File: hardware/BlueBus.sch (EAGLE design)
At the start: 76 parts

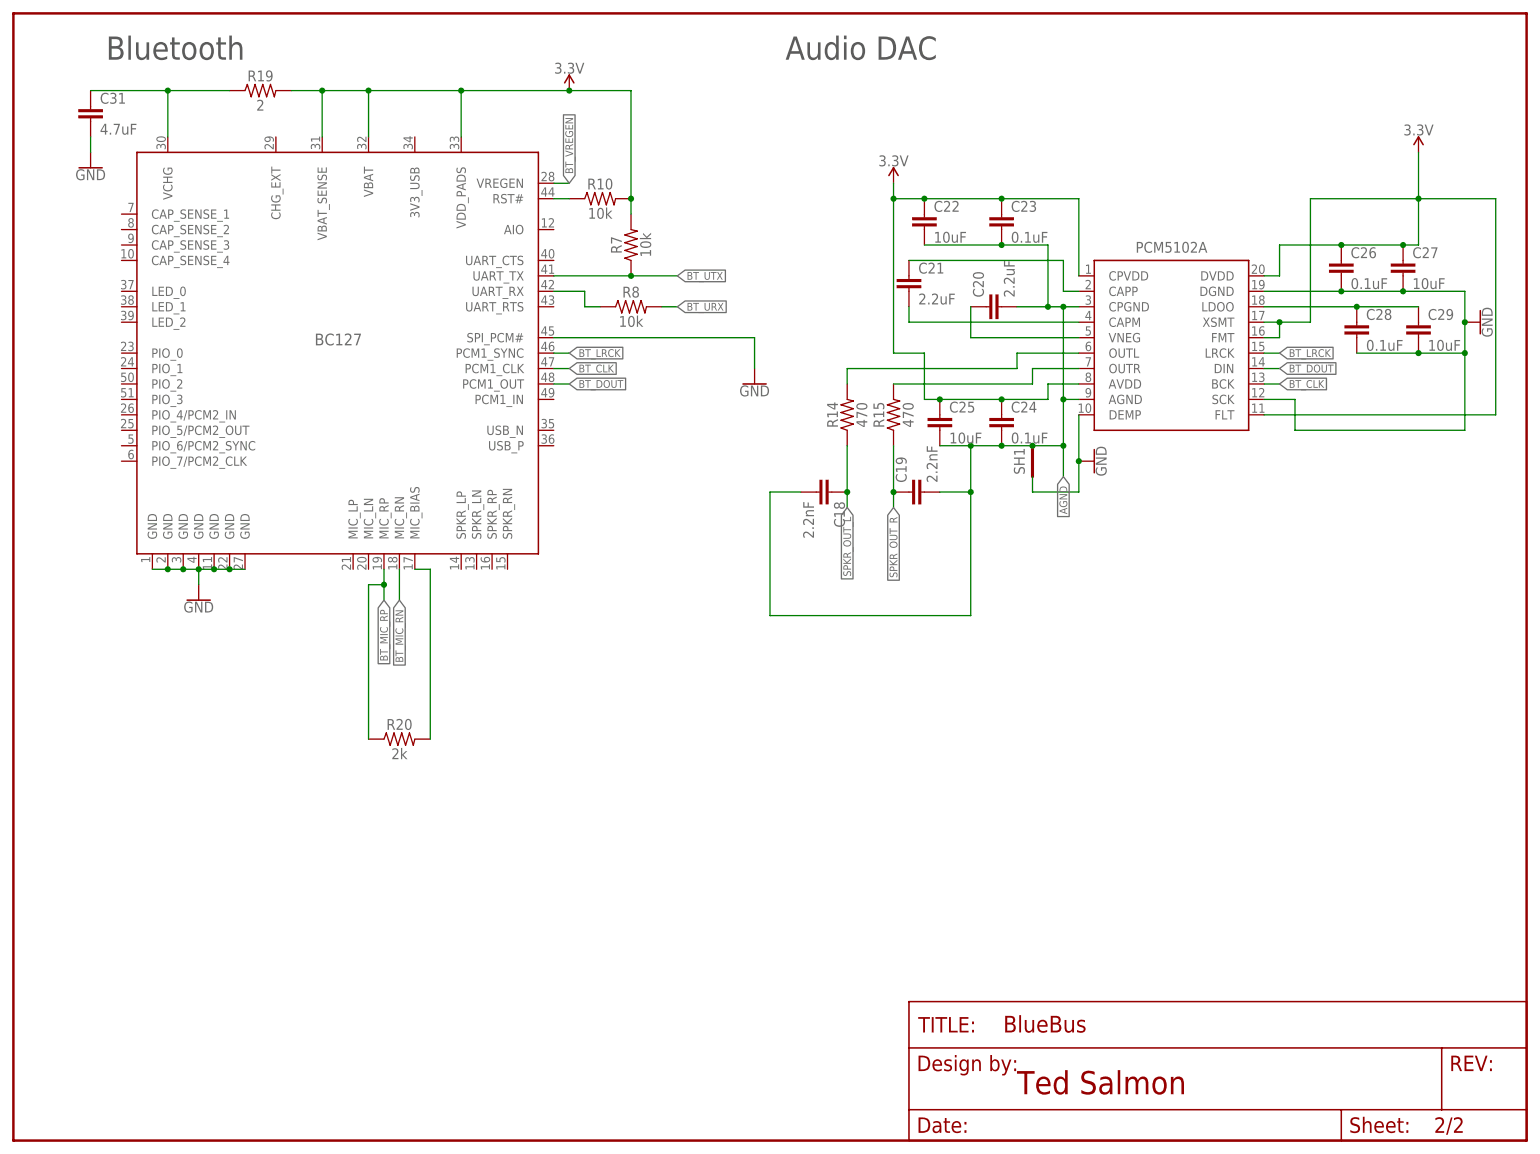
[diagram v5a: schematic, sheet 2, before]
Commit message: [IMP] hardware: MIC IN Fixes
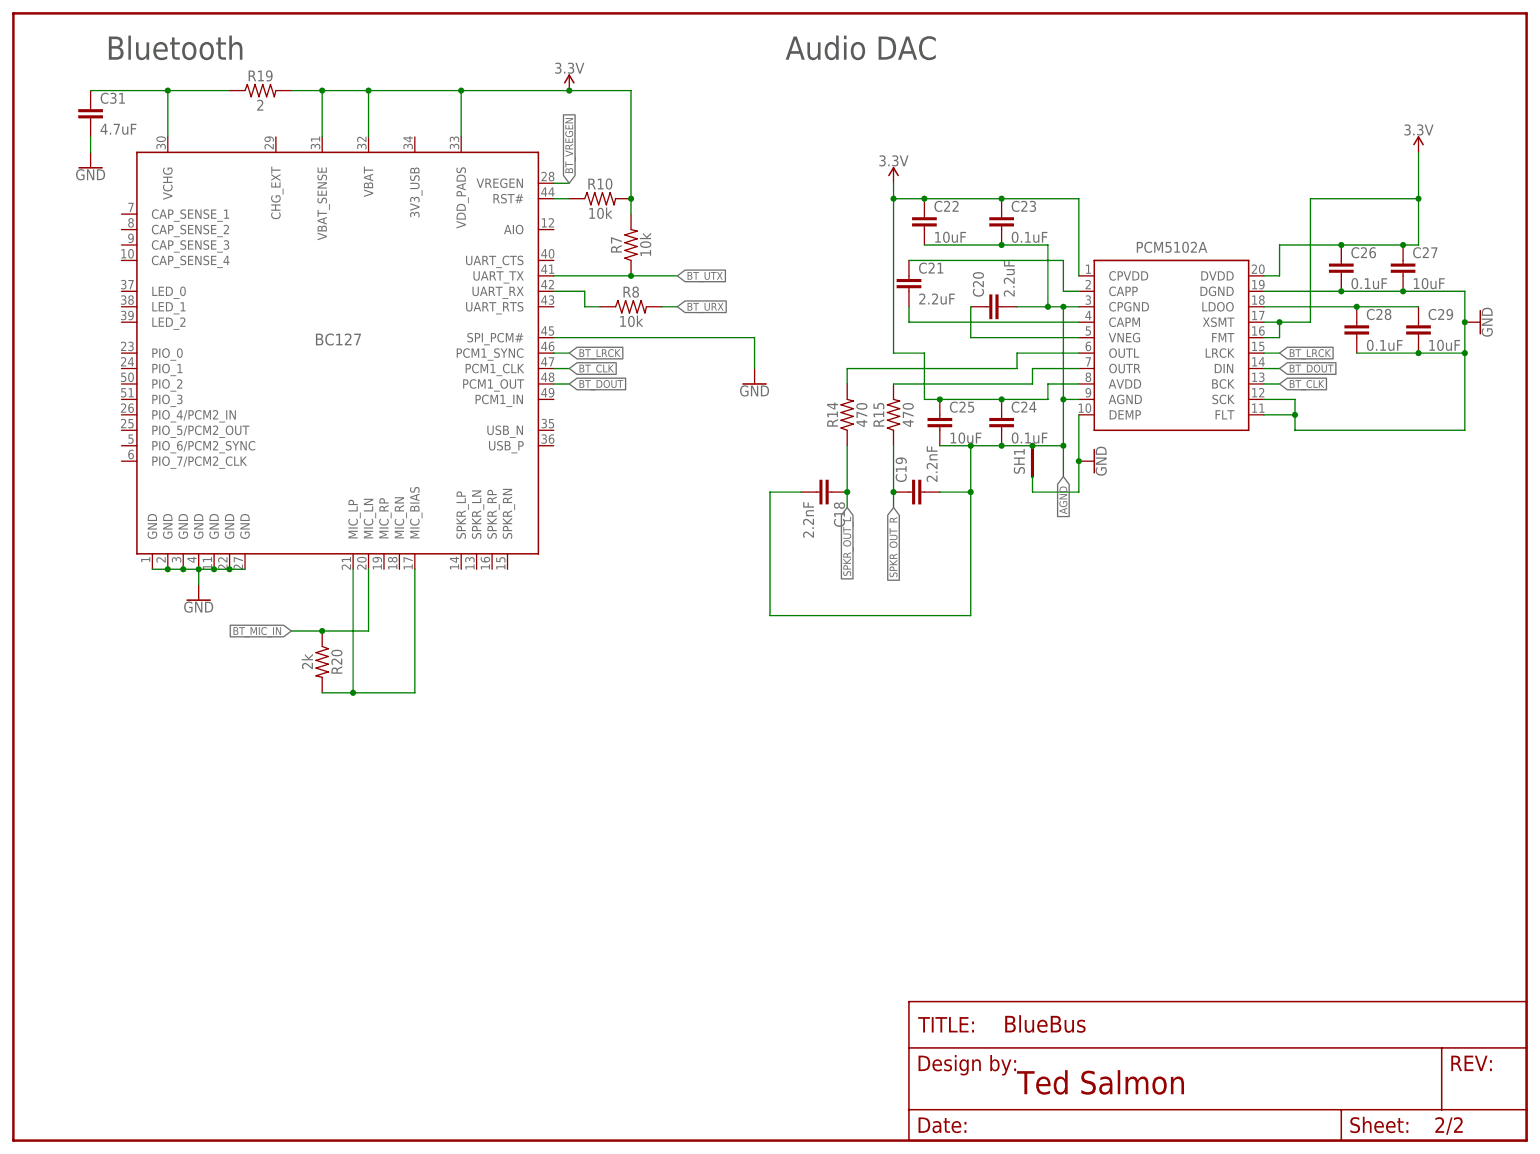
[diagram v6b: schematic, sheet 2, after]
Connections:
- removed net BT_MIC_BIAS: BC127.MIC_BIAS, R20.2
- removed net BT_MIC_RN: BC127.MIC_RN, MIC_IN.2
- removed net BT_MIC_RP: BC127.MIC_RP, MIC_IN.1, R20.1
- new net BT_MIC_IN: BC127.MIC_LN, MIC_IN.1, R20.1
- new net MIC_BIAS: BC127.MIC_BIAS, BC127.MIC_LP, R20.2
- net 3.3V: no longer PCM5102A.FLT
- net GND: now also MIC_IN.2, PCM5102A.FLT
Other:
- moved on the sheet: R20
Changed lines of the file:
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@@
 <junction x="220.98" y="30.48"/>
+</segment>
+<segment>
+<pinref part="MIC_IN" gate="G$1" pin="2"/>
+<wire x1="215.9" y1="167.64" x2="215.9" y2="165.1" width="0.1524" layer="91"/>
+<label x="215.9" y="165.1" size="1.27" layer="95" rot="R270" xref="yes"/>
 </segment>
 </net>
@@
 </segment>
 </net>
-<net name="BT_MIC_RP" class="0">
+<net name="BT_MIC_IN" class="0">
 <segment>
 <pinref part="MIC_IN" gate="G$1" pin="1"/>
 <wire x1="213.36" y1="167.64" x2="213.36" y2="165.1" width="0.1524" layer="91"/>
 <label x="213.36" y="165.1" size="1.27" layer="95" rot="R270" xref="yes"/>
-</segment>
-</net>
-<net name="BT_MIC_RN" class="0">
-<segment>
-<pinref part="MIC_IN" gate="G$1" pin="2"/>
-<wire x1="215.9" y1="167.64" x2="215.9" y2="165.1" width="0.1524" layer="91"/>
-<label x="215.9" y="165.1" size="1.27" layer="95" rot="R270" xref="yes"/>
 </segment>
 </net>
@@
 <attribute name="VALUE" x="103.124" y="147.32" size="1.778" layer="96" font="vector" rot="R90" align="top-center"/>
 </instance>
-<instance part="R20" gate="G$1" x="63.5" y="66.04" smashed="yes">
-<attribute name="NAME" x="63.5" y="67.564" size="1.778" layer="95" font="vector" align="bottom-center"/>
-<attribute name="VALUE" x="63.5" y="64.516" size="1.778" layer="96" font="vector" align="top-center"/>
+<instance part="R20" gate="G$1" x="50.8" y="78.74" smashed="yes" rot="R270">
+<attribute name="NAME" x="52.324" y="78.74" size="1.778" layer="95" font="vector" rot="R270" align="bottom-center"/>
+<attribute name="VALUE" x="49.276" y="78.74" size="1.778" layer="96" font="vector" rot="R270" align="top-center"/>
 </instance>
 <instance part="SUPPLY10" gate="G$1" x="91.44" y="172.72" smashed="yes">
@@
 <pinref part="PCM5102A" gate="G$1" pin="SCK"/>
 <wire x1="205.74" y1="121.92" x2="210.82" y2="121.92" width="0.1524" layer="91"/>
-<wire x1="210.82" y1="121.92" x2="210.82" y2="116.84" width="0.1524" layer="91"/>
+<wire x1="210.82" y1="121.92" x2="210.82" y2="119.38" width="0.1524" layer="91"/>
+<wire x1="210.82" y1="119.38" x2="210.82" y2="116.84" width="0.1524" layer="91"/>
 <wire x1="210.82" y1="116.84" x2="238.76" y2="116.84" width="0.1524" layer="91"/>
+<pinref part="PCM5102A" gate="G$1" pin="FLT"/>
+<wire x1="205.74" y1="119.38" x2="210.82" y2="119.38" width="0.1524" layer="91"/>
+<junction x="210.82" y="119.38"/>
 </segment>
 <segment>
@@
 </segment>
 </net>
-<net name="BT_MIC_RN" class="0">
-<segment>
-<pinref part="BC127" gate="G$1" pin="MIC_RN"/>
-<wire x1="63.5" y1="93.98" x2="63.5" y2="88.9" width="0.1524" layer="91"/>
-<label x="63.5" y="88.9" size="1.27" layer="95" rot="R270" xref="yes"/>
-</segment>
-</net>
-<net name="BT_MIC_BIAS" class="0">
-<segment>
-<pinref part="BC127" gate="G$1" pin="MIC_BIAS"/>
-<pinref part="R20" gate="G$1" pin="2"/>
-<wire x1="66.04" y1="93.98" x2="68.58" y2="93.98" width="0.1524" layer="91"/>
-<wire x1="68.58" y1="93.98" x2="68.58" y2="66.04" width="0.1524" layer="91"/>
-</segment>
-</net>
 <net name="BT_UTX" class="5">
 <segment>
@@
 <wire x1="106.68" y1="137.16" x2="109.22" y2="137.16" width="0.1524" layer="91"/>
 <label x="109.22" y="137.16" size="1.27" layer="95" xref="yes"/>
-</segment>
-</net>
-<net name="BT_MIC_RP" class="0">
-<segment>
-<pinref part="BC127" gate="G$1" pin="MIC_RP"/>
-<wire x1="60.96" y1="93.98" x2="60.96" y2="91.44" width="0.1524" layer="91"/>
-<pinref part="R20" gate="G$1" pin="1"/>
-<wire x1="58.42" y1="66.04" x2="58.42" y2="91.44" width="0.1524" layer="91"/>
-<wire x1="58.42" y1="91.44" x2="60.96" y2="91.44" width="0.1524" layer="91"/>
-<wire x1="60.96" y1="91.44" x2="60.96" y2="88.9" width="0.1524" layer="91"/>
-<junction x="60.96" y="91.44"/>
-<label x="60.96" y="88.9" size="1.27" layer="95" rot="R270" xref="yes"/>
 </segment>
 </net>
@@
 <wire x1="208.28" y1="132.08" x2="208.28" y2="134.62" width="0.1524" layer="91"/>
 <junction x="208.28" y="134.62"/>
-<pinref part="PCM5102A" gate="G$1" pin="FLT"/>
-<wire x1="205.74" y1="119.38" x2="243.84" y2="119.38" width="0.1524" layer="91"/>
-<wire x1="243.84" y1="119.38" x2="243.84" y2="154.94" width="0.1524" layer="91"/>
-<wire x1="243.84" y1="154.94" x2="231.14" y2="154.94" width="0.1524" layer="91"/>
 </segment>
 </net>
@@
 </segment>
 </net>
+<net name="MIC_BIAS" class="0">
+<segment>
+<pinref part="BC127" gate="G$1" pin="MIC_BIAS"/>
+<wire x1="66.04" y1="93.98" x2="66.04" y2="73.66" width="0.1524" layer="91"/>
+<wire x1="66.04" y1="73.66" x2="55.88" y2="73.66" width="0.1524" layer="91"/>
+<pinref part="BC127" gate="G$1" pin="MIC_LP"/>
+<wire x1="55.88" y1="93.98" x2="55.88" y2="73.66" width="0.1524" layer="91"/>
+<pinref part="R20" gate="G$1" pin="2"/>
+<wire x1="55.88" y1="73.66" x2="50.8" y2="73.66" width="0.1524" layer="91"/>
+<junction x="55.88" y="73.66"/>
+</segment>
+</net>
+<net name="BT_MIC_IN" class="0">
+<segment>
+<pinref part="BC127" gate="G$1" pin="MIC_LN"/>
+<wire x1="58.42" y1="93.98" x2="58.42" y2="83.82" width="0.1524" layer="91"/>
+<label x="45.72" y="83.82" size="1.27" layer="95" rot="R180" xref="yes"/>
+<pinref part="R20" gate="G$1" pin="1"/>
+<wire x1="58.42" y1="83.82" x2="50.8" y2="83.82" width="0.1524" layer="91"/>
+<wire x1="50.8" y1="83.82" x2="45.72" y2="83.82" width="0.1524" layer="91"/>
+<junction x="50.8" y="83.82"/>
+</segment>
+</net>
